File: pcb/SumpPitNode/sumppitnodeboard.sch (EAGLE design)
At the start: 41 parts, among them IC1 7805T

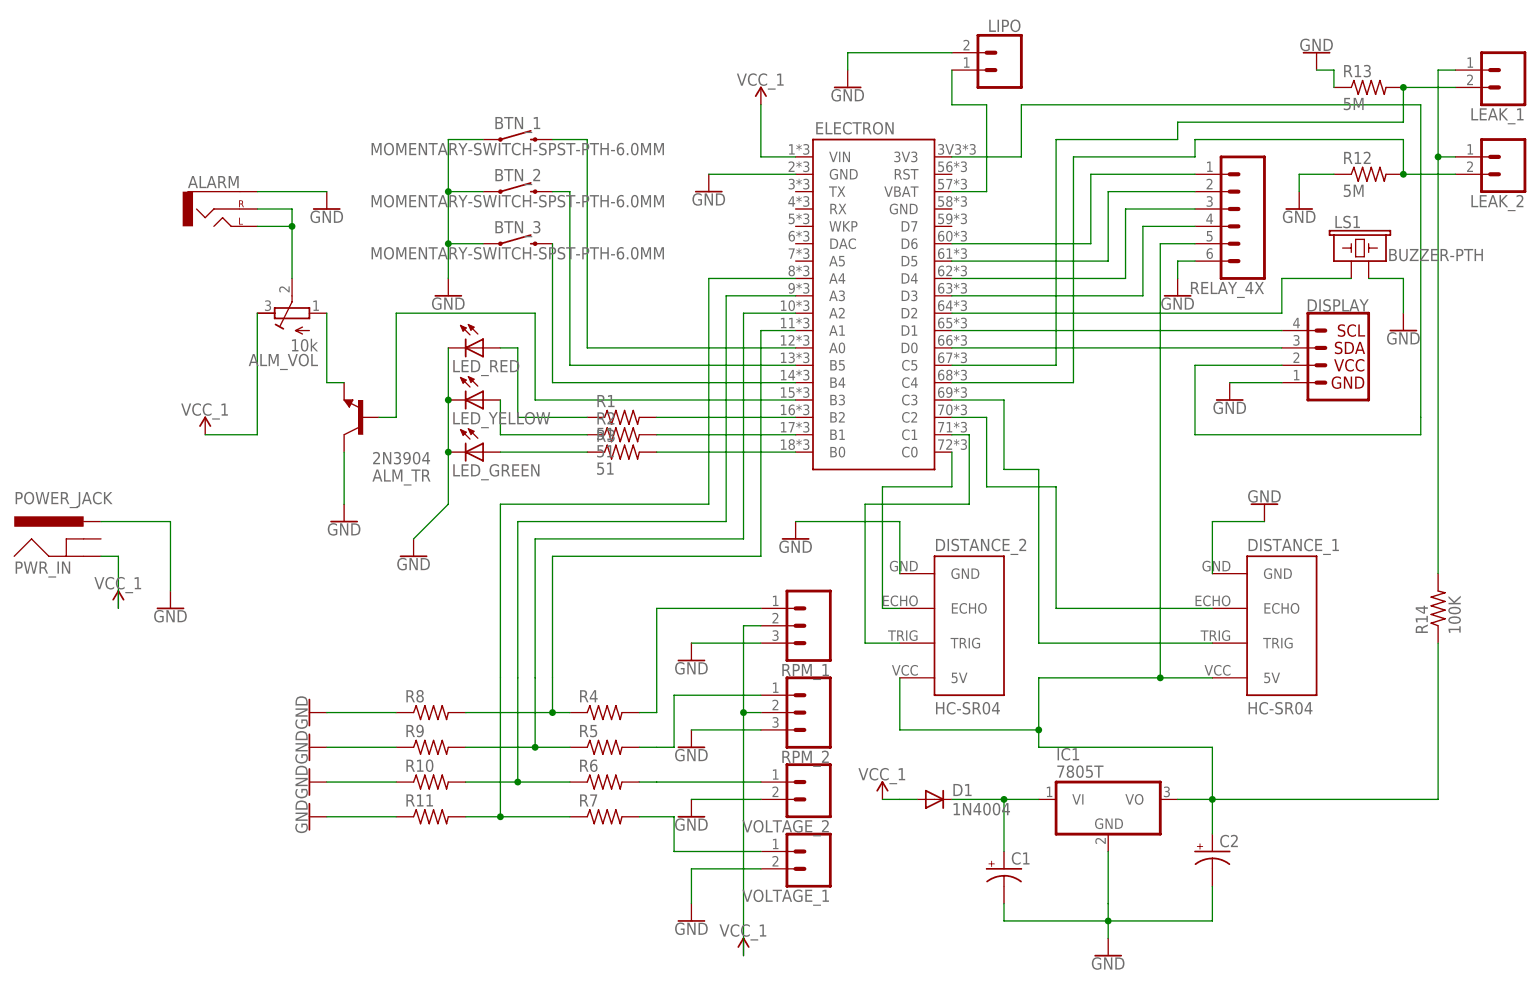
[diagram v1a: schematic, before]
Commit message: Reconnect leak sensors without pulldown.
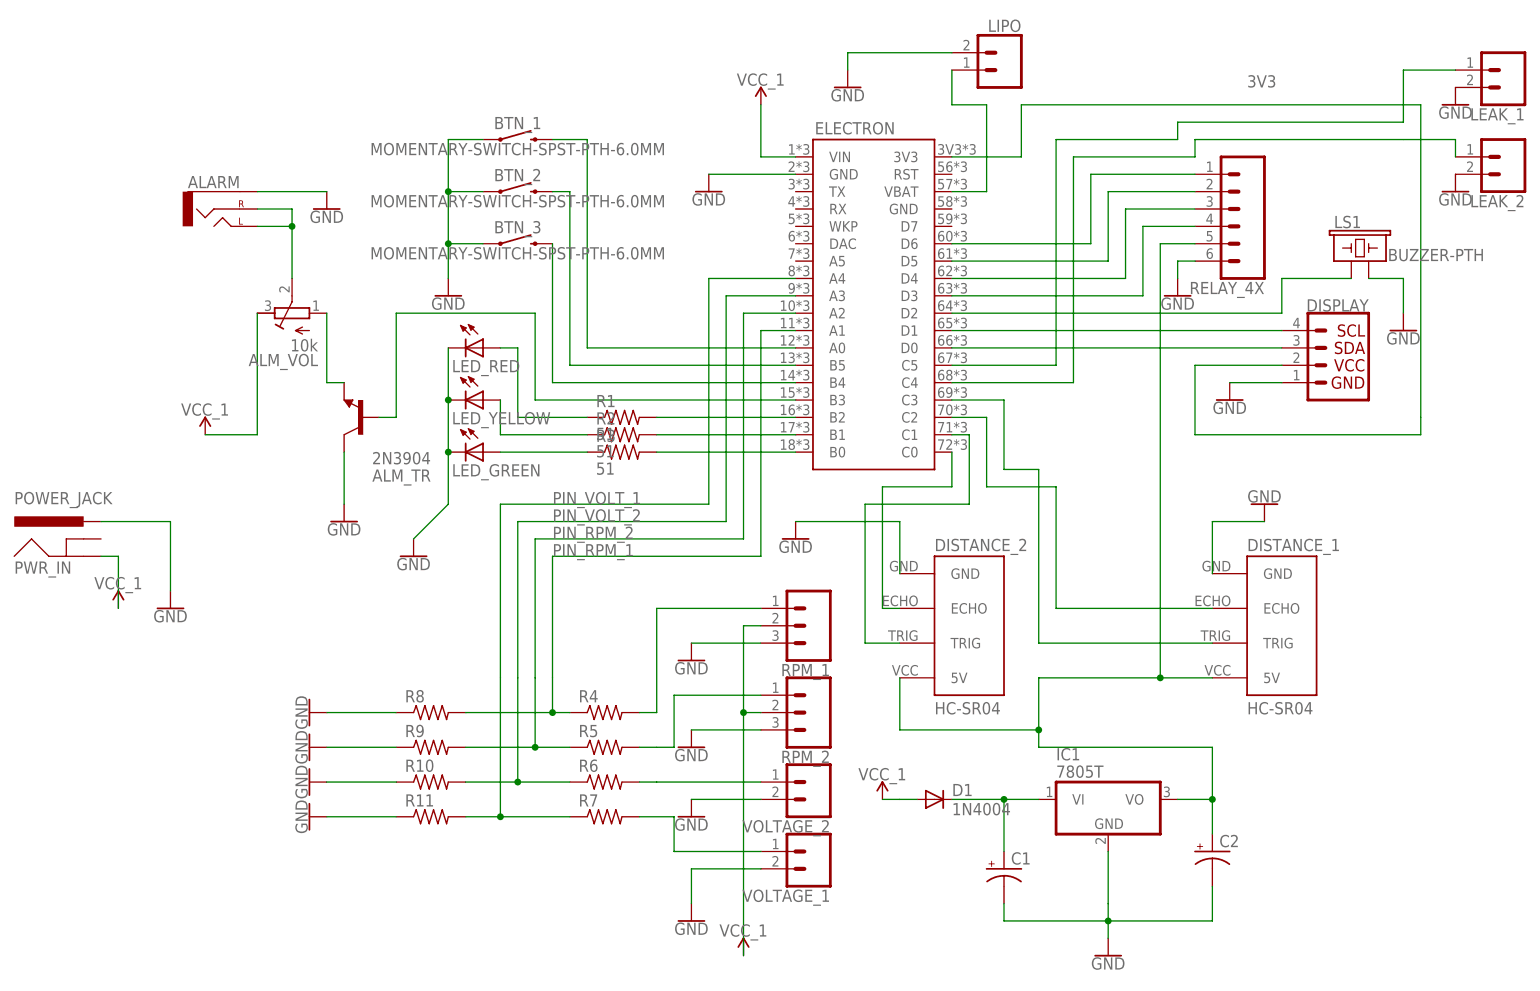
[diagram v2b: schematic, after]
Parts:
- removed R12, R13: 5M, resistor:R-US_0204/5
- removed R14: 100K, resistor:R-US_0204/5
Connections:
- net N$14 renamed 3V3
- net N$28 renamed PIN_RPM_1
- net N$29 renamed PIN_RPM_2
- net N$30 renamed PIN_VOLT_2
- net N$31 renamed PIN_VOLT_1
- removed net N$38: LEAK_1.1, LEAK_2.1, R14.2
- net GND: now also LEAK_1.2, LEAK_2.2; no longer R12.1, R13.1
- net N$23: now also LEAK_1.1; no longer LEAK_1.2, R13.2
- net N$32: now also LEAK_2.1; no longer LEAK_2.2, R12.2
- net N$33: no longer R14.1
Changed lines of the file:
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@@
 <part name="GND21" library="SparkFun-PowerSymbols" library_urn="urn:adsk.eagle:library:530" deviceset="GND" device=""/>
 <part name="VCC_12V4" library="SparkFun-PowerSymbols" library_urn="urn:adsk.eagle:library:530" deviceset="VCC_1" device=""/>
-<part name="R12" library="resistor" library_urn="urn:adsk.eagle:library:348" deviceset="R-US_" device="0204/5" package3d_urn="urn:adsk.eagle:package:25955/1" value="5M"/>
-<part name="R13" library="resistor" library_urn="urn:adsk.eagle:library:348" deviceset="R-US_" device="0204/5" package3d_urn="urn:adsk.eagle:package:25955/1" value="5M"/>
 <part name="GND22" library="SparkFun-PowerSymbols" library_urn="urn:adsk.eagle:library:530" deviceset="GND" device=""/>
 <part name="GND23" library="SparkFun-PowerSymbols" library_urn="urn:adsk.eagle:library:530" deviceset="GND" device=""/>
-<part name="R14" library="resistor" library_urn="urn:adsk.eagle:library:348" deviceset="R-US_" device="0204/5" package3d_urn="urn:adsk.eagle:package:25955/1" value="100K"/>
 </parts>
 <sheets>
@@
 <instance part="GND21" gate="1" x="-137.16" y="15.24"/>
 <instance part="VCC_12V4" gate="G$2" x="-144.78" y="15.24"/>
-<instance part="R12" gate="G$1" x="38.1" y="78.74"/>
-<instance part="R13" gate="G$1" x="38.1" y="91.44"/>
-<instance part="GND22" gate="1" x="30.48" y="96.52" rot="R180"/>
-<instance part="GND23" gate="1" x="27.94" y="73.66"/>
-<instance part="R14" gate="G$1" x="48.26" y="15.24" rot="R90"/>
+<instance part="GND22" gate="1" x="50.8" y="88.9"/>
+<instance part="GND23" gate="1" x="50.8" y="76.2"/>
 </instances>
 <busses>
@@
 </segment>
 <segment>
+<pinref part="GND22" gate="1" pin="GND"/>
+<pinref part="LEAK_1" gate="G$1" pin="2"/>
+</segment>
+<segment>
 <pinref part="GND23" gate="1" pin="GND"/>
-<pinref part="R12" gate="G$1" pin="1"/>
-<wire x1="27.94" y1="76.2" x2="27.94" y2="78.74" width="0.1524" layer="91"/>
-<wire x1="27.94" y1="78.74" x2="33.02" y2="78.74" width="0.1524" layer="91"/>
-</segment>
-<segment>
-<pinref part="R13" gate="G$1" pin="1"/>
-<pinref part="GND22" gate="1" pin="GND"/>
-<wire x1="33.02" y1="91.44" x2="33.02" y2="93.98" width="0.1524" layer="91"/>
-<wire x1="33.02" y1="93.98" x2="30.48" y2="93.98" width="0.1524" layer="91"/>
+<pinref part="LEAK_2" gate="G$1" pin="2"/>
 </segment>
 </net>
@@
 </segment>
 </net>
-<net name="N$14" class="0">
+<net name="3V3" class="0">
 <segment>
 <pinref part="DISPLAY" gate="G$1" pin="2"/>
@@
 <wire x1="-22.86" y1="81.28" x2="-12.7" y2="81.28" width="0.1524" layer="91"/>
 <wire x1="-12.7" y1="88.9" x2="-12.7" y2="81.28" width="0.1524" layer="91"/>
+<label x="20.32" y="91.44" size="1.778" layer="95"/>
 </segment>
 </net>
@@
 </segment>
 </net>
-<net name="N$28" class="0">
+<net name="PIN_RPM_1" class="0">
 <segment>
 <pinref part="R4" gate="G$1" pin="1"/>
@@
 <wire x1="-81.28" y1="0" x2="-93.98" y2="0" width="0.1524" layer="91"/>
 <junction x="-81.28" y="0"/>
-</segment>
-</net>
-<net name="N$29" class="0">
+<label x="-81.28" y="22.86" size="1.778" layer="95"/>
+</segment>
+</net>
+<net name="PIN_RPM_2" class="0">
 <segment>
 <pinref part="R5" gate="G$1" pin="1"/>
@@
 <pinref part="ELECTRON" gate="G$1" pin="A2"/>
 <wire x1="-53.34" y1="58.42" x2="-45.72" y2="58.42" width="0.1524" layer="91"/>
-</segment>
-</net>
-<net name="N$30" class="0">
+<label x="-81.28" y="25.4" size="1.778" layer="95"/>
+</segment>
+</net>
+<net name="PIN_VOLT_2" class="0">
 <segment>
 <pinref part="R6" gate="G$1" pin="1"/>
@@
 <pinref part="ELECTRON" gate="G$1" pin="A3"/>
 <wire x1="-55.88" y1="60.96" x2="-45.72" y2="60.96" width="0.1524" layer="91"/>
-</segment>
-</net>
-<net name="N$31" class="0">
+<label x="-81.28" y="27.94" size="1.778" layer="95"/>
+</segment>
+</net>
+<net name="PIN_VOLT_1" class="0">
 <segment>
 <pinref part="R7" gate="G$1" pin="1"/>
@@
 <junction x="-88.9" y="-15.24"/>
 <pinref part="R11" gate="G$1" pin="2"/>
+<label x="-81.28" y="30.48" size="1.778" layer="95"/>
 </segment>
 </net>
@@
 <wire x1="7.62" y1="68.58" x2="7.62" y2="5.08" width="0.1524" layer="91"/>
 <junction x="7.62" y="5.08"/>
-<wire x1="15.24" y1="-12.7" x2="48.26" y2="-12.7" width="0.1524" layer="91"/>
-<wire x1="48.26" y1="-12.7" x2="48.26" y2="10.16" width="0.1524" layer="91"/>
-<pinref part="R14" gate="G$1" pin="1"/>
 </segment>
 </net>
@@
 <net name="N$23" class="0">
 <segment>
-<pinref part="LEAK_1" gate="G$1" pin="2"/>
-<pinref part="R13" gate="G$1" pin="2"/>
-<wire x1="50.8" y1="91.44" x2="43.18" y2="91.44" width="0.1524" layer="91"/>
-<wire x1="43.18" y1="91.44" x2="43.18" y2="86.36" width="0.1524" layer="91"/>
-<junction x="43.18" y="91.44"/>
 <wire x1="43.18" y1="86.36" x2="10.16" y2="86.36" width="0.1524" layer="91"/>
 <wire x1="10.16" y1="86.36" x2="10.16" y2="83.82" width="0.1524" layer="91"/>
@@
 <pinref part="ELECTRON" gate="G$1" pin="C5"/>
 <wire x1="-7.62" y1="50.8" x2="-22.86" y2="50.8" width="0.1524" layer="91"/>
+<wire x1="43.18" y1="86.36" x2="43.18" y2="93.98" width="0.1524" layer="91"/>
+<pinref part="LEAK_1" gate="G$1" pin="1"/>
+<wire x1="43.18" y1="93.98" x2="50.8" y2="93.98" width="0.1524" layer="91"/>
 </segment>
 </net>
 <net name="N$32" class="0">
 <segment>
-<pinref part="LEAK_2" gate="G$1" pin="2"/>
-<pinref part="R12" gate="G$1" pin="2"/>
-<wire x1="50.8" y1="78.74" x2="43.18" y2="78.74" width="0.1524" layer="91"/>
-<wire x1="43.18" y1="78.74" x2="43.18" y2="83.82" width="0.1524" layer="91"/>
-<junction x="43.18" y="78.74"/>
 <wire x1="43.18" y1="83.82" x2="12.7" y2="83.82" width="0.1524" layer="91"/>
 <wire x1="12.7" y1="83.82" x2="12.7" y2="81.28" width="0.1524" layer="91"/>
@@
 <pinref part="ELECTRON" gate="G$1" pin="C4"/>
 <wire x1="-5.08" y1="48.26" x2="-22.86" y2="48.26" width="0.1524" layer="91"/>
-</segment>
-</net>
-<net name="N$38" class="0">
-<segment>
-<pinref part="LEAK_1" gate="G$1" pin="1"/>
-<wire x1="48.26" y1="93.98" x2="50.8" y2="93.98" width="0.1524" layer="91"/>
 <pinref part="LEAK_2" gate="G$1" pin="1"/>
-<wire x1="48.26" y1="81.28" x2="50.8" y2="81.28" width="0.1524" layer="91"/>
-<wire x1="48.26" y1="81.28" x2="48.26" y2="93.98" width="0.1524" layer="91"/>
-<junction x="48.26" y="81.28"/>
-<wire x1="48.26" y1="20.32" x2="48.26" y2="81.28" width="0.1524" layer="91"/>
-<pinref part="R14" gate="G$1" pin="2"/>
-</segment>
-</net>
+<wire x1="43.18" y1="83.82" x2="50.8" y2="83.82" width="0.1524" layer="91"/>
+<wire x1="50.8" y1="83.82" x2="50.8" y2="81.28" width="0.1524" layer="91"/>
+</segment>
+</net>

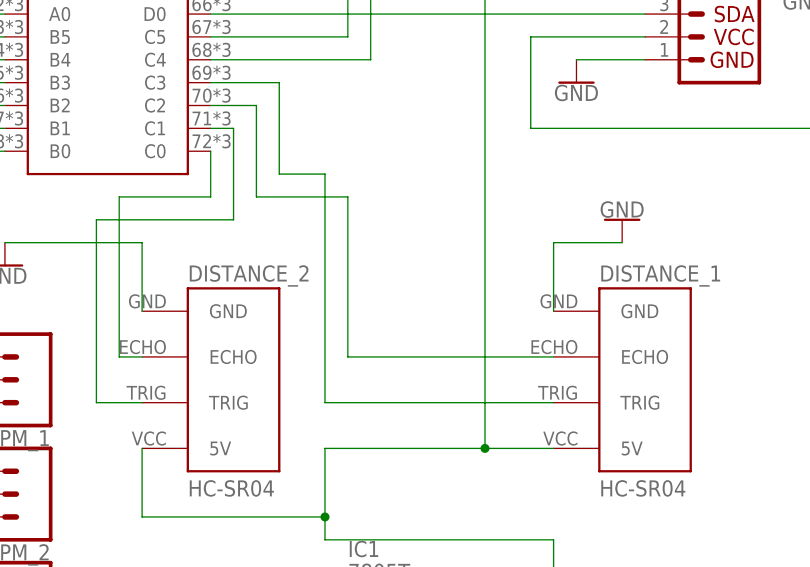
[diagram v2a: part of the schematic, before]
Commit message: Add 470ohm voltage divider to echo pin of distance 1 input. Leave the 2nd distancce input directly connected.
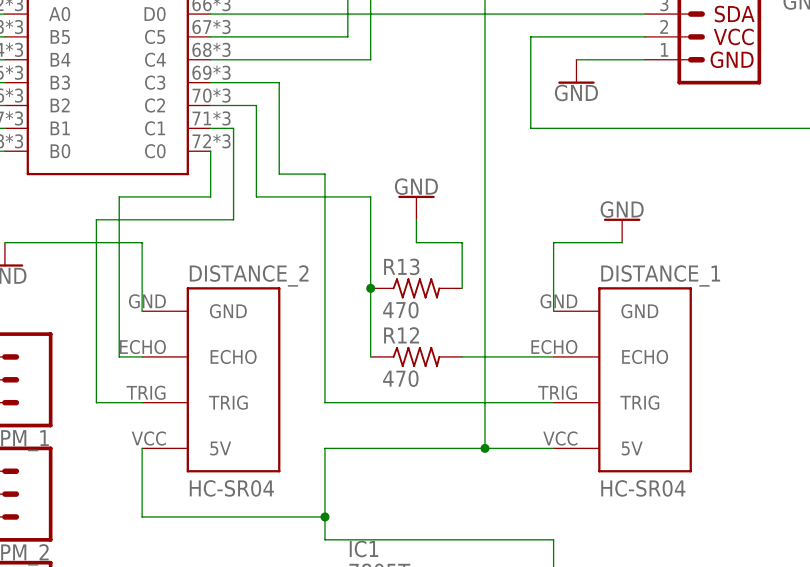
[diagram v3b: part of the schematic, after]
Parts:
- added R12, R13: 470, resistor:R-US_0204/5
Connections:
- removed net N$13: DISTANCE_1.ECHO, ELECTRON.C2
- new net N$14: DISTANCE_1.ECHO, R12.2
- new net N$28: ELECTRON.C2, R12.1, R13.1
- net GND: now also R13.2
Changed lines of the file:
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@@
 <part name="GND22" library="SparkFun-PowerSymbols" library_urn="urn:adsk.eagle:library:530" deviceset="GND" device=""/>
 <part name="GND23" library="SparkFun-PowerSymbols" library_urn="urn:adsk.eagle:library:530" deviceset="GND" device=""/>
+<part name="R12" library="resistor" library_urn="urn:adsk.eagle:library:348" deviceset="R-US_" device="0204/5" package3d_urn="urn:adsk.eagle:package:25955/1" value="470"/>
+<part name="R13" library="resistor" library_urn="urn:adsk.eagle:library:348" deviceset="R-US_" device="0204/5" package3d_urn="urn:adsk.eagle:package:25955/1" value="470"/>
+<part name="GND24" library="SparkFun-PowerSymbols" library_urn="urn:adsk.eagle:library:530" deviceset="GND" device=""/>
 </parts>
 <sheets>
@@
 <instance part="GND22" gate="1" x="50.8" y="88.9"/>
 <instance part="GND23" gate="1" x="50.8" y="76.2"/>
+<instance part="R12" gate="G$1" x="0" y="15.24"/>
+<instance part="R13" gate="G$1" x="0" y="22.86"/>
+<instance part="GND24" gate="1" x="0" y="33.02" rot="R180"/>
 </instances>
 <busses>
@@
 <pinref part="LEAK_2" gate="G$1" pin="2"/>
 </segment>
+<segment>
+<pinref part="R13" gate="G$1" pin="2"/>
+<wire x1="5.08" y1="22.86" x2="5.08" y2="27.94" width="0.1524" layer="91"/>
+<wire x1="5.08" y1="27.94" x2="0" y2="27.94" width="0.1524" layer="91"/>
+<wire x1="0" y1="27.94" x2="0" y2="30.48" width="0.1524" layer="91"/>
+<pinref part="GND24" gate="1" pin="GND"/>
+</segment>
 </net>
 <net name="N$2" class="0">
@@
 <wire x1="-12.7" y1="88.9" x2="-12.7" y2="81.28" width="0.1524" layer="91"/>
 <label x="20.32" y="91.44" size="1.778" layer="95"/>
-</segment>
-</net>
-<net name="N$13" class="0">
-<segment>
-<pinref part="DISTANCE_1" gate="J_ULTRASONIC" pin="ECHO"/>
-<wire x1="15.24" y1="15.24" x2="-7.62" y2="15.24" width="0.1524" layer="91"/>
-<wire x1="-7.62" y1="15.24" x2="-7.62" y2="33.02" width="0.1524" layer="91"/>
-<wire x1="-7.62" y1="33.02" x2="-17.78" y2="33.02" width="0.1524" layer="91"/>
-<wire x1="-17.78" y1="33.02" x2="-17.78" y2="43.18" width="0.1524" layer="91"/>
-<pinref part="ELECTRON" gate="G$1" pin="C2"/>
-<wire x1="-22.86" y1="43.18" x2="-17.78" y2="43.18" width="0.1524" layer="91"/>
 </segment>
 </net>
@@
 </segment>
 </net>
+<net name="N$14" class="0">
+<segment>
+<pinref part="DISTANCE_1" gate="J_ULTRASONIC" pin="ECHO"/>
+<pinref part="R12" gate="G$1" pin="2"/>
+<wire x1="15.24" y1="15.24" x2="5.08" y2="15.24" width="0.1524" layer="91"/>
+</segment>
+</net>
+<net name="N$28" class="0">
+<segment>
+<pinref part="R12" gate="G$1" pin="1"/>
+<pinref part="R13" gate="G$1" pin="1"/>
+<wire x1="-5.08" y1="15.24" x2="-5.08" y2="22.86" width="0.1524" layer="91"/>
+<wire x1="-5.08" y1="22.86" x2="-5.08" y2="33.02" width="0.1524" layer="91"/>
+<junction x="-5.08" y="22.86"/>
+<wire x1="-5.08" y1="33.02" x2="-17.78" y2="33.02" width="0.1524" layer="91"/>
+<wire x1="-17.78" y1="33.02" x2="-17.78" y2="43.18" width="0.1524" layer="91"/>
+<pinref part="ELECTRON" gate="G$1" pin="C2"/>
+<wire x1="-22.86" y1="43.18" x2="-17.78" y2="43.18" width="0.1524" layer="91"/>
+</segment>
+</net>

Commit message: Save project.
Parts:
- removed LED_GREEN, LED_RED, LED_YELLOW: (no value), led:LED3MM
- added BIGLED_G, BIGLED_R, BIGLED_Y: (no value), SparkFun-Connectors:CONN_02
- added G_TR, R_TR, Y_TR: 2N3904, transistor:2N3904
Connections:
- new net N$13: BIGLED_G.2, G_TR.E
- new net N$29: BIGLED_Y.2, Y_TR.E
- new net N$30: BIGLED_R.2, R_TR.E
- net GND: now also G_TR.C, R_TR.C, Y_TR.C; no longer LED_GREEN.C, LED_RED.C, LED_YELLOW.C
- net N$20: now also Y_TR.B; no longer LED_YELLOW.A
- net N$21: now also G_TR.B; no longer LED_GREEN.A
- net N$4: now also R_TR.B; no longer LED_RED.A
- net VCC_1: now also BIGLED_G.1, BIGLED_R.1, BIGLED_Y.1
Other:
- moved on the sheet: ALM_TR, PWR_IN
